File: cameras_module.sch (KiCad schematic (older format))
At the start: 22 parts, among them J2 WE_68715014522, U5 NTS0102GT, U6 PCA9547BS

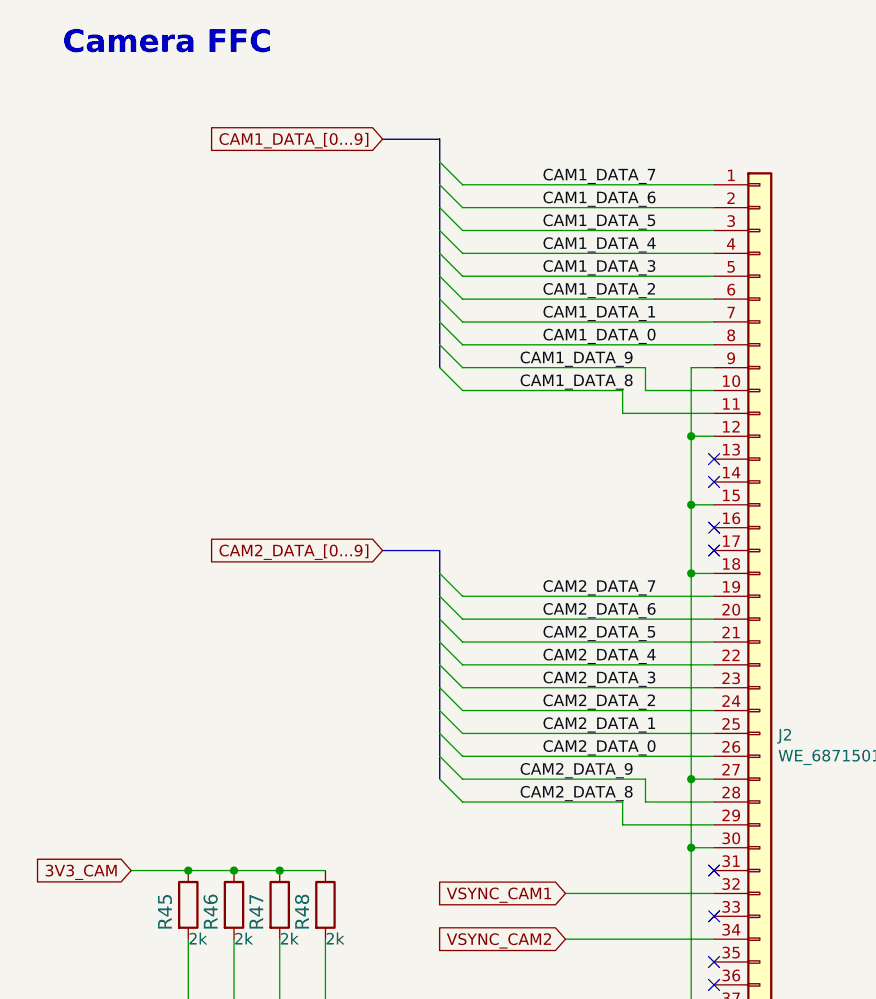
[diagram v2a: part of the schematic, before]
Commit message: FFC and general display camera connectors distributed on board
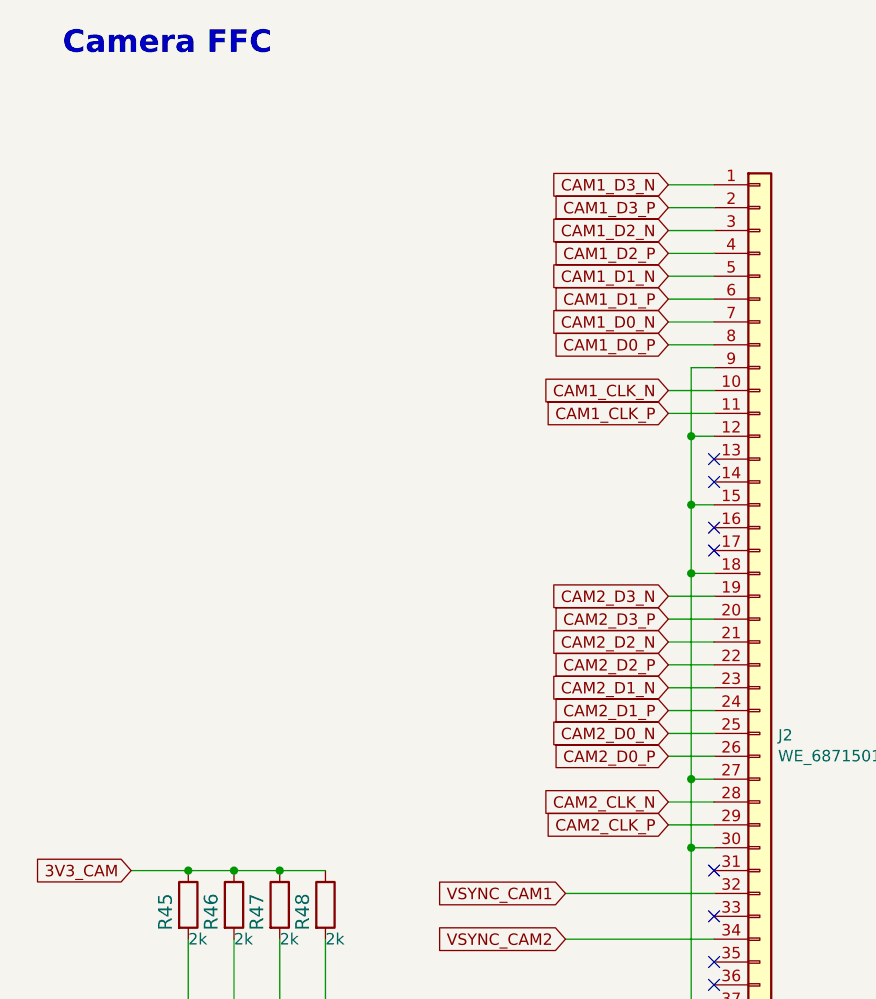
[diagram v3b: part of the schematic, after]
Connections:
- net CAM1_DATA_0 renamed CAM1_D0_P
- net CAM1_DATA_1 renamed CAM1_D0_N
- net CAM1_DATA_2 renamed CAM1_D1_P
- net CAM1_DATA_3 renamed CAM1_D1_N
- net CAM1_DATA_4 renamed CAM1_D2_P
- net CAM1_DATA_5 renamed CAM1_D2_N
- net CAM1_DATA_6 renamed CAM1_D3_P
- net CAM1_DATA_7 renamed CAM1_D3_N
- net CAM1_DATA_8 renamed CAM1_CLK_P
- net CAM1_DATA_9 renamed CAM1_CLK_N
- net CAM2_DATA_0 renamed CAM2_D0_P
- net CAM2_DATA_1 renamed CAM2_D0_N
- net CAM2_DATA_2 renamed CAM2_D1_P
- net CAM2_DATA_3 renamed CAM2_D1_N
- net CAM2_DATA_4 renamed CAM2_D2_P
- net CAM2_DATA_5 renamed CAM2_D2_N
- net CAM2_DATA_6 renamed CAM2_D3_P
- net CAM2_DATA_7 renamed CAM2_D3_N
- net CAM2_DATA_8 renamed CAM2_CLK_P
- net CAM2_DATA_9 renamed CAM2_CLK_N
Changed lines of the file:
@@
 Wire Wire Line
 	11950 5600 12600 5600
-Entry Wire Line
-	11400 2200 11500 2300
-Entry Wire Line
-	11400 2300 11500 2400
-Entry Wire Line
-	11400 2400 11500 2500
-Entry Wire Line
-	11400 2500 11500 2600
-Entry Wire Line
-	11400 2600 11500 2700
-Entry Wire Line
-	11400 2700 11500 2800
-Entry Wire Line
-	11400 2800 11500 2900
-Entry Wire Line
-	11400 2900 11500 3000
-Entry Wire Line
-	11400 3000 11500 3100
-Entry Wire Line
-	11400 3100 11500 3200
-Wire Wire Line
-	11500 2900 12600 2900
-Wire Wire Line
-	12600 3000 11500 3000
-Wire Wire Line
-	11500 2700 12600 2700
-Wire Wire Line
-	12600 2800 11500 2800
-Wire Wire Line
-	11500 2500 12600 2500
-Wire Wire Line
-	12600 2600 11500 2600
-Wire Wire Line
-	11500 2300 12600 2300
-Wire Wire Line
-	12600 2400 11500 2400
-Wire Wire Line
-	12600 3200 12300 3200
-Wire Wire Line
-	12300 3200 12300 3100
-Wire Wire Line
-	12300 3100 11500 3100
-Wire Wire Line
-	12600 3300 12200 3300
-Wire Wire Line
-	12200 3300 12200 3200
-Wire Wire Line
-	12200 3200 11500 3200
-Text Label 11850 2900 0    50   ~ 0
-CAM1_DATA_1
-Text Label 11850 3000 0    50   ~ 0
-CAM1_DATA_0
-Text Label 11850 2700 0    50   ~ 0
-CAM1_DATA_3
-Text Label 11850 2800 0    50   ~ 0
-CAM1_DATA_2
-Text Label 11850 2500 0    50   ~ 0
-CAM1_DATA_5
-Text Label 11850 2600 0    50   ~ 0
-CAM1_DATA_4
-Text Label 11850 2300 0    50   ~ 0
-CAM1_DATA_7
-Text Label 11850 2400 0    50   ~ 0
-CAM1_DATA_6
-Text Label 11750 3100 0    50   ~ 0
-CAM1_DATA_9
-Text Label 11750 3200 0    50   ~ 0
-CAM1_DATA_8
-Text GLabel 11150 2100 0    50   Input ~ 0
-CAM1_DATA_[0...9]
-Wire Bus Line
-	11400 2100 11150 2100
-Entry Wire Line
-	11400 4000 11500 4100
-Entry Wire Line
-	11400 4100 11500 4200
-Entry Wire Line
-	11400 4200 11500 4300
-Entry Wire Line
-	11400 4300 11500 4400
-Entry Wire Line
-	11400 4400 11500 4500
-Entry Wire Line
-	11400 4500 11500 4600
-Entry Wire Line
-	11400 4600 11500 4700
-Entry Wire Line
-	11400 4700 11500 4800
-Entry Wire Line
-	11400 4800 11500 4900
-Entry Wire Line
-	11400 4900 11500 5000
-Wire Wire Line
-	11500 4700 12600 4700
-Wire Wire Line
-	12600 4800 11500 4800
-Wire Wire Line
-	11500 4500 12600 4500
-Wire Wire Line
-	12600 4600 11500 4600
-Wire Wire Line
-	11500 4300 12600 4300
-Wire Wire Line
-	12600 4400 11500 4400
-Wire Wire Line
-	11500 4100 12600 4100
-Wire Wire Line
-	12600 4200 11500 4200
-Wire Wire Line
-	12600 5000 12300 5000
-Wire Wire Line
-	12300 5000 12300 4900
-Wire Wire Line
-	12300 4900 11500 4900
-Wire Wire Line
-	12600 5100 12200 5100
-Wire Wire Line
-	12200 5100 12200 5000
-Wire Wire Line
-	12200 5000 11500 5000
-Text Label 11850 4700 0    50   ~ 0
-CAM2_DATA_1
-Text Label 11850 4800 0    50   ~ 0
-CAM2_DATA_0
-Text Label 11850 4500 0    50   ~ 0
-CAM2_DATA_3
-Text Label 11850 4600 0    50   ~ 0
-CAM2_DATA_2
-Text Label 11850 4300 0    50   ~ 0
-CAM2_DATA_5
-Text Label 11850 4400 0    50   ~ 0
-CAM2_DATA_4
-Text Label 11850 4100 0    50   ~ 0
-CAM2_DATA_7
-Text Label 11850 4200 0    50   ~ 0
-CAM2_DATA_6
-Text Label 11750 4900 0    50   ~ 0
-CAM2_DATA_9
-Text Label 11750 5000 0    50   ~ 0
-CAM2_DATA_8
-Text GLabel 11150 3900 0    50   Input ~ 0
-CAM2_DATA_[0...9]
-Wire Bus Line
-	11400 3900 11150 3900
 $Comp
 L sc606-baseboard:NTS0102GT U5
@@
 Wire Wire Line
 	4450 8450 4450 8800
-Wire Bus Line
-	11400 2100 11400 3100
-Wire Bus Line
-	11400 3900 11400 4900
+Text GLabel 12400 3000 0    50   Input ~ 0
+CAM1_D0_P
+Text GLabel 12400 2900 0    50   Input ~ 0
+CAM1_D0_N
+Text GLabel 12400 2800 0    50   Input ~ 0
+CAM1_D1_P
+Text GLabel 12400 2700 0    50   Input ~ 0
+CAM1_D1_N
+Text GLabel 12400 2600 0    50   Input ~ 0
+CAM1_D2_P
+Text GLabel 12400 2500 0    50   Input ~ 0
+CAM1_D2_N
+Text GLabel 12400 2400 0    50   Input ~ 0
+CAM1_D3_P
+Text GLabel 12400 2300 0    50   Input ~ 0
+CAM1_D3_N
+Text GLabel 12400 3300 0    50   Input ~ 0
+CAM1_CLK_P
+Text GLabel 12400 3200 0    50   Input ~ 0
+CAM1_CLK_N
+Wire Wire Line
+	12400 2300 12600 2300
+Wire Wire Line
+	12600 2400 12400 2400
+Wire Wire Line
+	12400 2500 12600 2500
+Wire Wire Line
+	12600 2600 12400 2600
+Wire Wire Line
+	12600 2700 12400 2700
+Wire Wire Line
+	12400 2800 12600 2800
+Wire Wire Line
+	12600 2900 12400 2900
+Wire Wire Line
+	12400 3000 12600 3000
+Wire Wire Line
+	12600 3200 12400 3200
+Wire Wire Line
+	12400 3300 12600 3300
+Text GLabel 12400 4800 0    50   Input ~ 0
+CAM2_D0_P
+Text GLabel 12400 4700 0    50   Input ~ 0
+CAM2_D0_N
+Text GLabel 12400 4600 0    50   Input ~ 0
+CAM2_D1_P
+Text GLabel 12400 4500 0    50   Input ~ 0
+CAM2_D1_N
+Text GLabel 12400 4400 0    50   Input ~ 0
+CAM2_D2_P
+Text GLabel 12400 4300 0    50   Input ~ 0
+CAM2_D2_N
+Text GLabel 12400 4200 0    50   Input ~ 0
+CAM2_D3_P
+Text GLabel 12400 4100 0    50   Input ~ 0
+CAM2_D3_N
+Text GLabel 12400 5100 0    50   Input ~ 0
+CAM2_CLK_P
+Text GLabel 12400 5000 0    50   Input ~ 0
+CAM2_CLK_N
+Wire Wire Line
+	12400 4100 12600 4100
+Wire Wire Line
+	12600 4200 12400 4200
+Wire Wire Line
+	12400 4300 12600 4300
+Wire Wire Line
+	12600 4400 12400 4400
+Wire Wire Line
+	12400 4500 12600 4500
+Wire Wire Line
+	12600 4600 12400 4600
+Wire Wire Line
+	12400 4700 12600 4700
+Wire Wire Line
+	12600 4800 12400 4800
+Wire Wire Line
+	12400 5000 12600 5000
+Wire Wire Line
+	12600 5100 12400 5100
 $EndSCHEMATC

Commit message: Connecting LT9611
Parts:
- U6: footprint sc606-baseboard-footprints:VQFN-24 -> antmicro-footprints:HVQFN24
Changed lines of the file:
@@
 F 0 "U6" H 4850 6089 60  0000 C CNN
 F 1 "PCA9547BS" H 4850 5983 60  0000 C CNN
-F 2 "sc606-baseboard-footprints:VQFN-24" H 4700 3300 60  0001 C CNN
+F 2 "antmicro-footprints:HVQFN24" H 4700 3300 60  0001 C CNN
 F 3 "https://www.nxp.com/docs/en/data-sheet/PCA9547.pdf" H 4950 4700 60  0001 C CNN
 F 4 " NXP" H 4950 4700 50  0001 C CNN "Manufacturer"

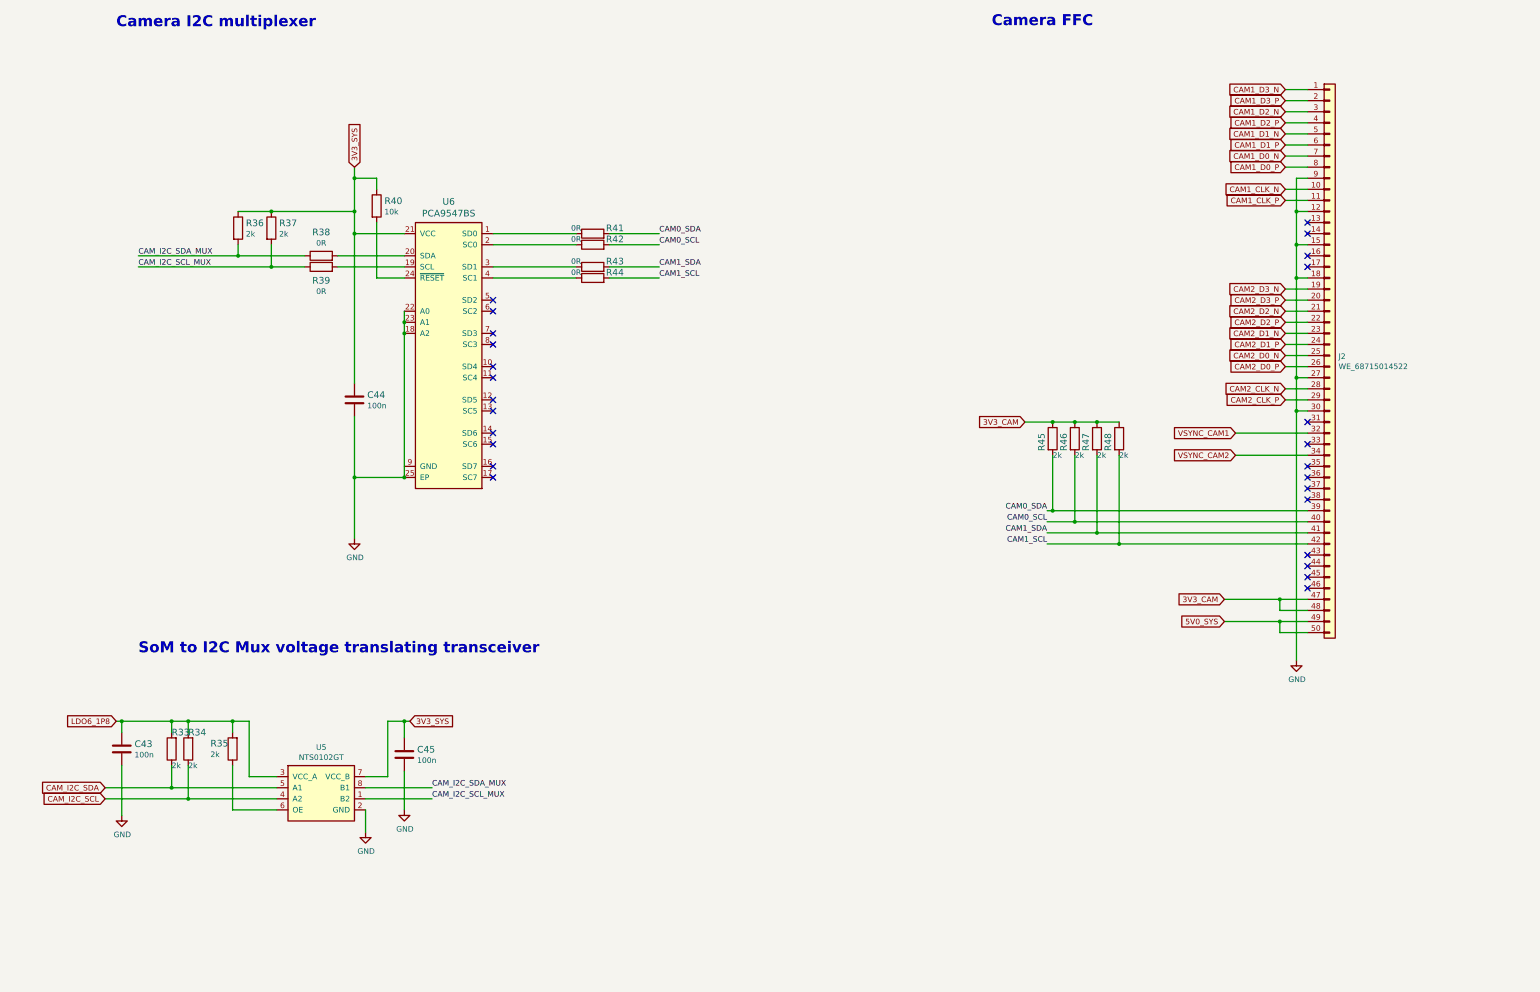
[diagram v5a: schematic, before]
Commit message: Cleaned and added testpoints to cameras_module.sch
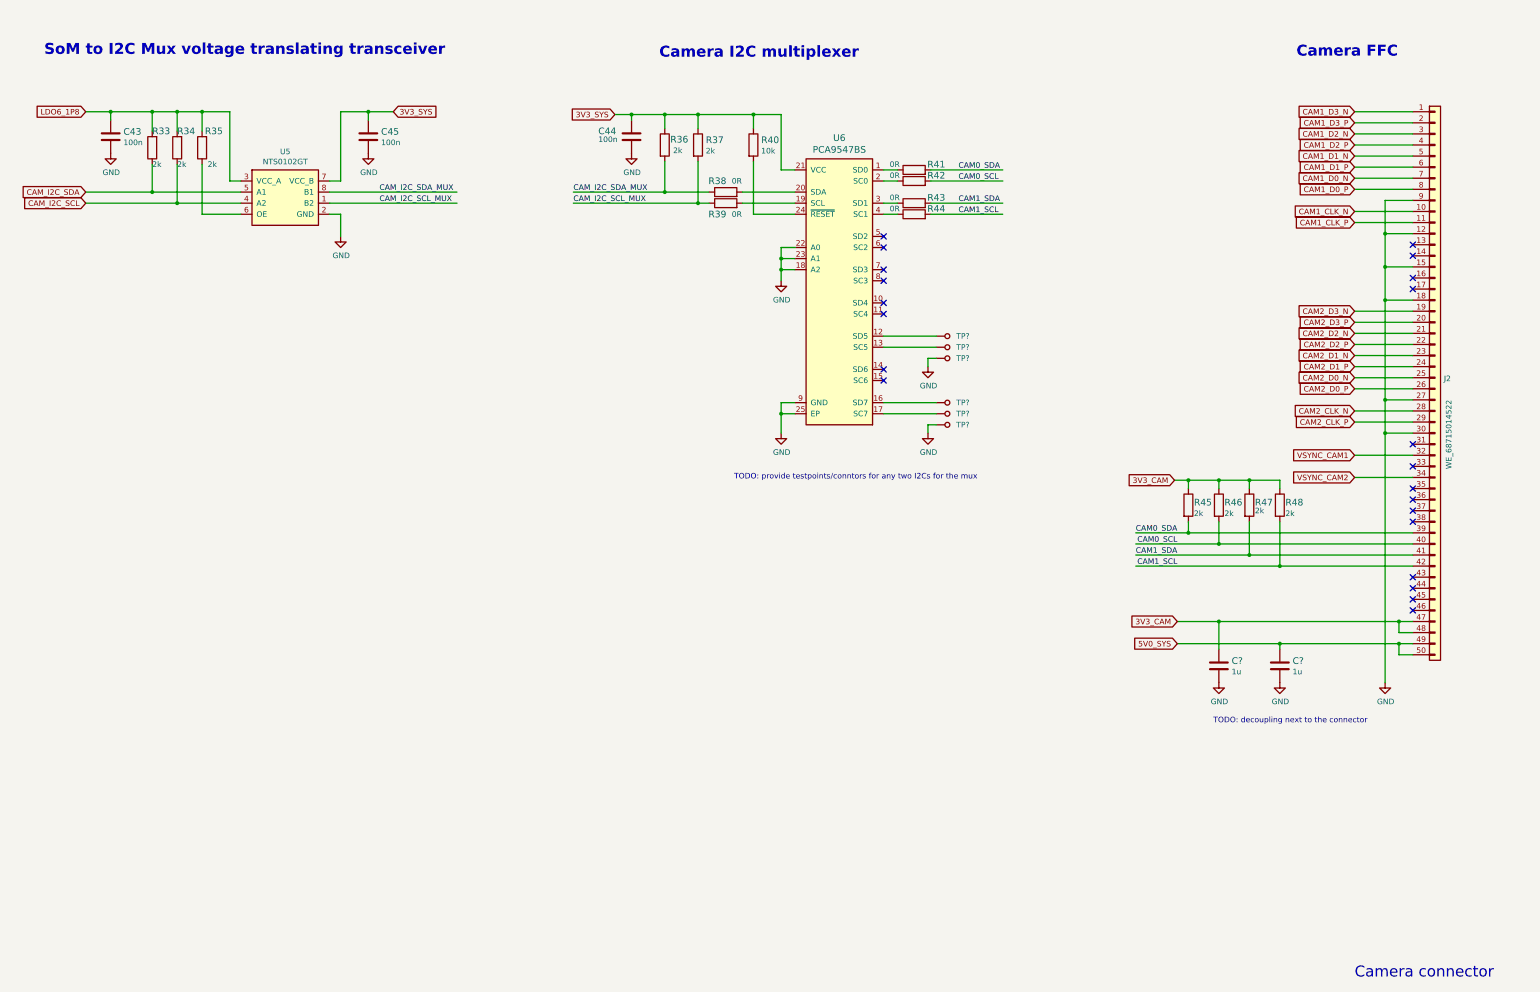
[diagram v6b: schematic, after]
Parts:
- added C? (x2): C_1u_0402, sc606-baseboard-footprints:0402-cap, symbol sc606-baseboard:C_1u_0402
- added TP? (x6): TP_SMD_0_75MM, sc606-baseboard-footprints:Testpoint_smd_0_75mm, symbol sc606-baseboard:TP_SMD_0_75MM
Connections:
- wire segments 120 -> 141
- no-connect marks 26 -> 22
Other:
- note added: "Camera connector\n"
- note added: "TODO: decoupling next to the connector"
- note added: "TODO: provide testpoints/conntors for any two I2Cs for the mux"
- moved on the sheet: C43, C44, C45, J2, R33, R34, R35, R36, R37, R38, R39, R40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
